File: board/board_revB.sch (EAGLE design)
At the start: 78 parts, among them Q1 ULN2003AS, Q2 ULN2003AD, Y1 8Mhz

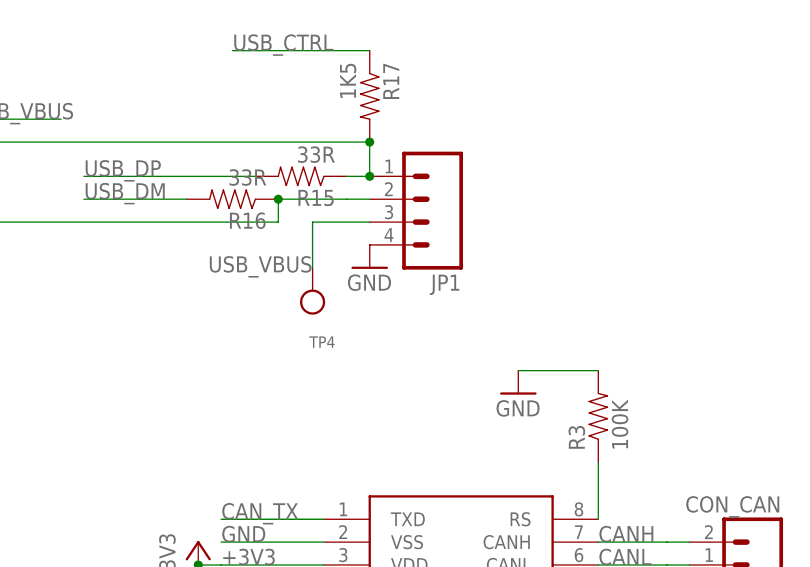
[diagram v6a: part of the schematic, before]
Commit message: [Board Rev B] USB connector renamed.
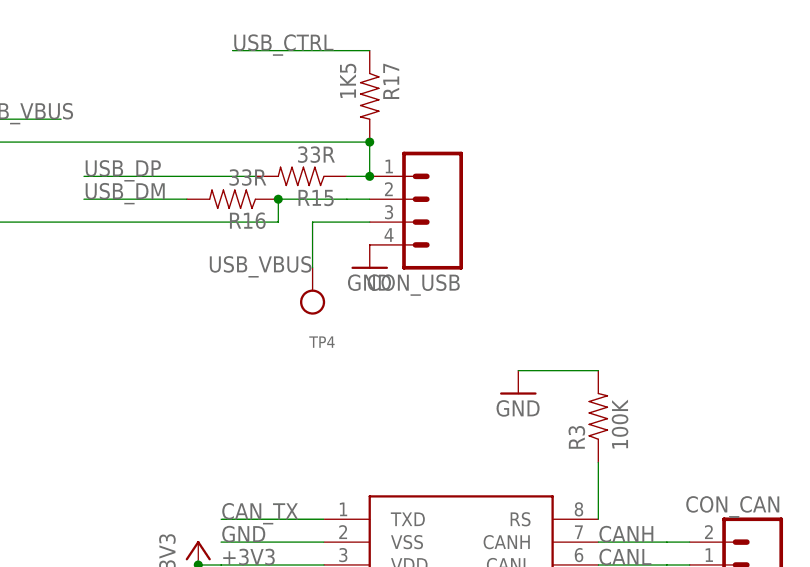
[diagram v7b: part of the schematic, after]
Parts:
- renumbered JP1 to CON_USB
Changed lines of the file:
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@@
 <part name="R22" library="SparkFun-Resistors" deviceset="RESISTOR" device="0603-RES" value="56R"/>
 <part name="R21" library="SparkFun-Resistors" deviceset="RESISTOR" device="0603-RES" value="56R"/>
-<part name="JP1" library="SparkFun-Connectors" deviceset="M04" device="LOCK"/>
+<part name="CON_USB" library="SparkFun-Connectors" deviceset="M04" device="LOCK"/>
 <part name="TP2" library="microbuilder" deviceset="TESTPOINT" device="ROUND1MM"/>
 <part name="TP4" library="microbuilder" deviceset="TESTPOINT" device="ROUND1MM"/>
@@
 <instance part="R22" gate="G$1" x="233.68" y="179.07" rot="R180"/>
 <instance part="R21" gate="G$1" x="242.57" y="176.53" rot="R180"/>
-<instance part="JP1" gate="G$1" x="300.99" y="125.73" rot="R180"/>
+<instance part="CON_USB" gate="G$1" x="300.99" y="125.73" rot="R180"/>
 <instance part="TP2" gate="G$1" x="74.93" y="22.86"/>
 <instance part="TP4" gate="G$1" x="289.56" y="118.11" rot="R180"/>
@@
 <segment>
 <pinref part="GND8" gate="1" pin="GND"/>
-<pinref part="JP1" gate="G$1" pin="4"/>
+<pinref part="CON_USB" gate="G$1" pin="4"/>
 </segment>
 </net>
@@
 <label x="289.56" y="119.38" size="1.778" layer="95" rot="R180"/>
 <wire x1="289.56" y1="123.19" x2="289.56" y2="118.11" width="0.1524" layer="91"/>
-<pinref part="JP1" gate="G$1" pin="3"/>
+<pinref part="CON_USB" gate="G$1" pin="3"/>
 <pinref part="TP4" gate="G$1" pin="P$1"/>
 </segment>
@@
 <wire x1="251.46" y1="129.54" x2="251.46" y2="123.19" width="0.1524" layer="91"/>
 <wire x1="251.46" y1="123.19" x2="285.75" y2="123.19" width="0.1524" layer="91"/>
-<pinref part="JP1" gate="G$1" pin="2"/>
+<pinref part="CON_USB" gate="G$1" pin="2"/>
 </segment>
 </net>
@@
 <wire x1="226.06" y1="132.08" x2="295.91" y2="132.08" width="0.1524" layer="91"/>
 <junction x="295.91" y="132.08"/>
-<pinref part="JP1" gate="G$1" pin="1"/>
+<pinref part="CON_USB" gate="G$1" pin="1"/>
 <junction x="295.91" y="128.27"/>
 </segment>

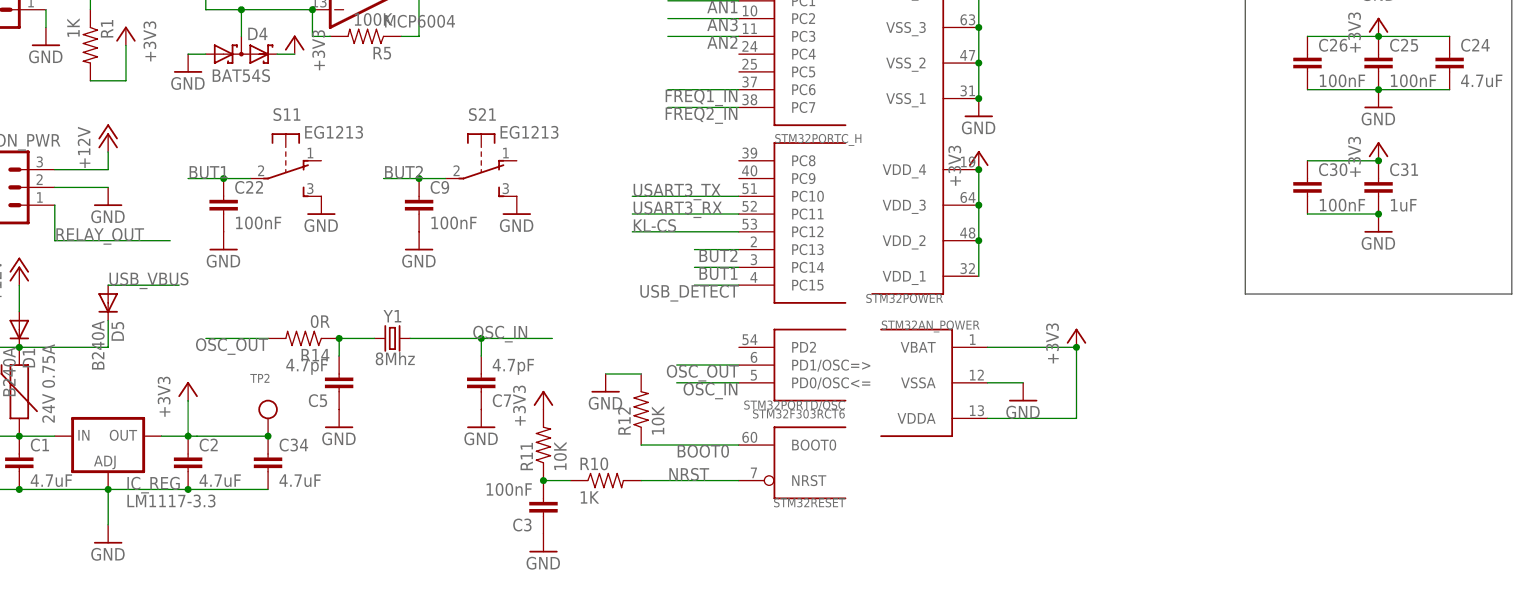
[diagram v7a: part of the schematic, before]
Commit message: [Board Rev B] Adding voltage reference for VDDA.
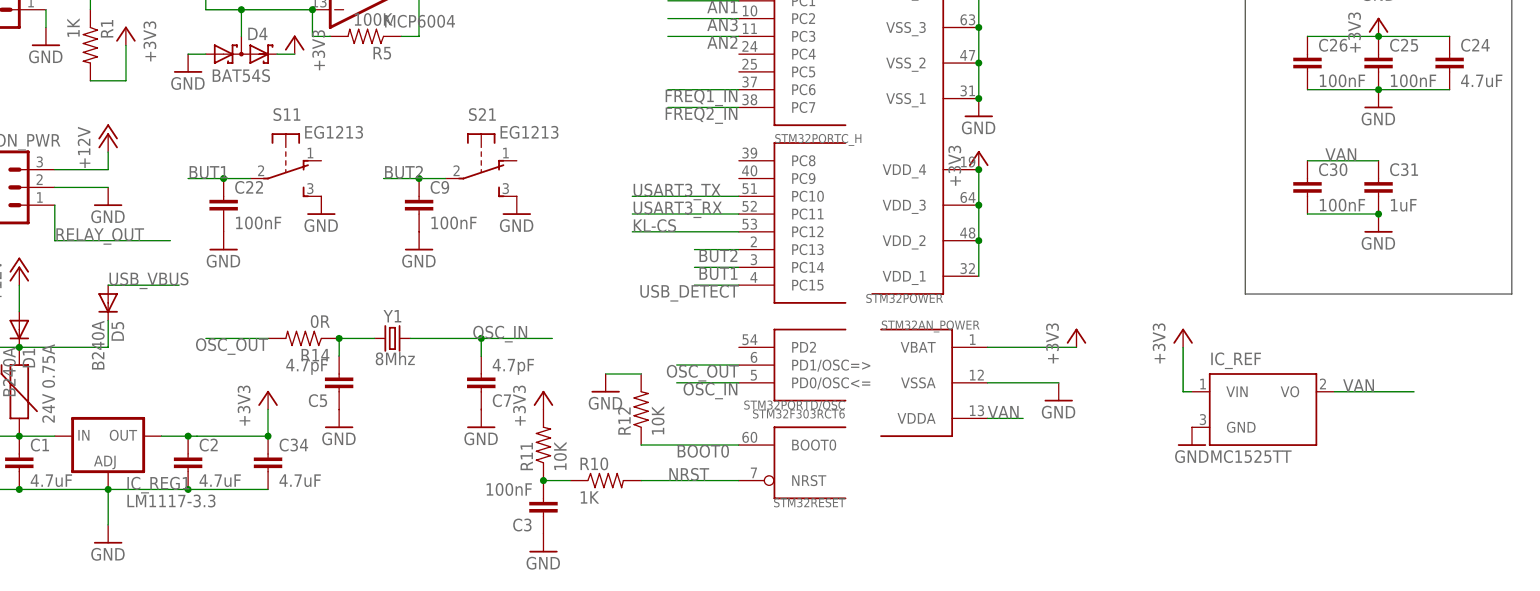
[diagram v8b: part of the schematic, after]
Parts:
- removed TP2: (no value), microbuilder:TESTPOINTROUND1MM
- added IC_REF: MC1525TT, microchip:MC1525TT
- renumbered IC_REG to IC_REG1
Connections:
- new net VAN: C30.1, C31.1, IC_REF.VO, STM32AN_POWER.VDDA
- net +3V3: now also IC_REF.VIN; no longer C30.1, C31.1, STM32AN_POWER.VDDA, TP2.P$1
- net GND: now also IC_REF.GND
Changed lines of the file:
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@@
 </classes>
 <parts>
-<part name="IC_REG" library="v-reg" deviceset="LD117A?*" device="DT" technology="33TR" value="LM1117-3.3"/>
+<part name="IC_REG1" library="v-reg" deviceset="LD117A?*" device="DT" technology="33TR" value="LM1117-3.3"/>
 <part name="GND1" library="supply1" deviceset="GND" device=""/>
-<part name="+3V1" library="supply1" deviceset="+3V3" device=""/>
 <part name="C1" library="SparkFun-Passives" deviceset="CAP" device="0603-CAP" value="4.7uF"/>
 <part name="C2" library="SparkFun-Passives" deviceset="CAP" device="0603-CAP" value="4.7uF"/>
@@
 <part name="C31" library="SparkFun-Capacitors" deviceset="CAP" device="0603-CAP" value="1uF"/>
 <part name="GND33" library="supply1" deviceset="GND" device=""/>
-<part name="+3V15" library="supply1" deviceset="+3V3" device=""/>
 <part name="CON_DBG" library="SparkFun-Connectors" deviceset="M03X2" device="2X3_SILK_SM"/>
 <part name="IC_OPA" library="linear" deviceset="LMV324?*" device="MZ" value="MCP6004"/>
@@
 <part name="R21" library="SparkFun-Resistors" deviceset="RESISTOR" device="0603-RES" value="56R"/>
 <part name="CON_USB" library="SparkFun-Connectors" deviceset="M04" device="LOCK"/>
-<part name="TP2" library="microbuilder" deviceset="TESTPOINT" device="ROUND1MM"/>
 <part name="TP4" library="microbuilder" deviceset="TESTPOINT" device="ROUND1MM"/>
 <part name="F1" library="misc" deviceset="PTC" device="1812K" value="24V 0.75A"/>
+<part name="IC_REF" library="microchip" deviceset="MC15*" device="TT" technology="25"/>
+<part name="GND22" library="supply1" deviceset="GND" device=""/>
+<part name="+3V1" library="supply1" deviceset="+3V3" device=""/>
+<part name="+3V6" library="supply1" deviceset="+3V3" device=""/>
 </parts>
 <sheets>
@@
 </plain>
 <instances>
-<instance part="IC_REG" gate="G$1" x="52.07" y="22.86"/>
+<instance part="IC_REG1" gate="G$1" x="52.07" y="22.86"/>
 <instance part="GND1" gate="1" x="52.07" y="7.62"/>
-<instance part="+3V1" gate="G$1" x="63.5" y="30.48"/>
 <instance part="C1" gate="G$1" x="39.37" y="17.78"/>
 <instance part="C2" gate="G$1" x="63.5" y="17.78"/>
@@
 <instance part="C31" gate="G$1" x="233.68" y="57.15"/>
 <instance part="GND33" gate="1" x="233.68" y="52.07"/>
-<instance part="+3V15" gate="G$1" x="233.68" y="64.77"/>
 <instance part="CON_DBG" gate="G$1" x="133.35" y="152.4"/>
 <instance part="IC_OPA" gate="P" x="110.49" y="114.3"/>
@@
 <instance part="IC_OPA" gate="A" x="87.63" y="148.59"/>
 <instance part="IC_OPA" gate="B" x="73.66" y="106.68"/>
-<instance part="GND3" gate="1" x="182.88" y="27.94"/>
+<instance part="GND3" gate="1" x="187.96" y="27.94"/>
 <instance part="GND7" gate="1" x="44.45" y="113.03"/>
 <instance part="+3V2" gate="G$1" x="190.5" y="38.1"/>
@@
 <instance part="R21" gate="G$1" x="242.57" y="176.53" rot="R180"/>
 <instance part="CON_USB" gate="G$1" x="300.99" y="125.73" rot="R180"/>
-<instance part="TP2" gate="G$1" x="74.93" y="22.86"/>
 <instance part="TP4" gate="G$1" x="289.56" y="118.11" rot="R180"/>
 <instance part="F1" gate="G$1" x="39.37" y="27.94" rot="R90"/>
+<instance part="IC_REF" gate="G$1" x="217.17" y="26.67"/>
+<instance part="GND22" gate="1" x="207.01" y="21.59"/>
+<instance part="+3V1" gate="G$1" x="205.74" y="38.1"/>
+<instance part="+3V6" gate="G$1" x="74.93" y="29.21"/>
 </instances>
 <busses>
@@
 <net name="GND" class="0">
 <segment>
-<pinref part="IC_REG" gate="G$1" pin="ADJ"/>
+<pinref part="IC_REG1" gate="G$1" pin="ADJ"/>
 <wire x1="52.07" y1="15.24" x2="52.07" y2="10.16" width="0.1524" layer="91"/>
 <pinref part="GND1" gate="1" pin="GND"/>
@@
 <pinref part="GND3" gate="1" pin="GND"/>
 <pinref part="STM32" gate="AN_POWER" pin="VSSA"/>
-<wire x1="182.88" y1="30.48" x2="177.8" y2="30.48" width="0.1524" layer="91"/>
+<wire x1="187.96" y1="30.48" x2="177.8" y2="30.48" width="0.1524" layer="91"/>
 </segment>
 <segment>
@@
 <pinref part="CON_USB" gate="G$1" pin="4"/>
 </segment>
+<segment>
+<pinref part="IC_REF" gate="G$1" pin="GND"/>
+<pinref part="GND22" gate="1" pin="GND"/>
+</segment>
 </net>
 <net name="+3V3" class="0">
-<segment>
-<pinref part="IC_REG" gate="G$1" pin="OUT"/>
-<wire x1="59.69" y1="22.86" x2="63.5" y2="22.86" width="0.1524" layer="91"/>
-<pinref part="+3V1" gate="G$1" pin="+3V3"/>
-<wire x1="63.5" y1="27.94" x2="63.5" y2="22.86" width="0.1524" layer="91"/>
-<pinref part="C2" gate="G$1" pin="1"/>
-<junction x="63.5" y="22.86"/>
-<pinref part="C34" gate="G$1" pin="1"/>
-<wire x1="64.77" y1="22.86" x2="74.93" y2="22.86" width="0.1524" layer="91"/>
-<wire x1="64.77" y1="22.86" x2="63.5" y2="22.86" width="0.1524" layer="91"/>
-<pinref part="TP2" gate="G$1" pin="P$1"/>
-<junction x="74.93" y="22.86"/>
-</segment>
 <segment>
 <pinref part="C24" gate="G$1" pin="1"/>
@@
 <junction x="233.68" y="97.79"/>
 <pinref part="C28" gate="G$1" pin="1"/>
-</segment>
-<segment>
-<pinref part="C30" gate="G$1" pin="1"/>
-<pinref part="C31" gate="G$1" pin="1"/>
-<wire x1="223.52" y1="62.23" x2="233.68" y2="62.23" width="0.1524" layer="91"/>
-<pinref part="+3V15" gate="G$1" pin="+3V3"/>
-<junction x="233.68" y="62.23"/>
 </segment>
 <segment>
@@
 </segment>
 <segment>
-<pinref part="STM32" gate="AN_POWER" pin="VDDA"/>
-<wire x1="177.8" y1="25.4" x2="190.5" y2="25.4" width="0.1524" layer="91"/>
+<pinref part="+3V1" gate="G$1" pin="+3V3"/>
+<pinref part="IC_REF" gate="G$1" pin="VIN"/>
+<wire x1="207.01" y1="29.21" x2="205.74" y2="29.21" width="0.1524" layer="91"/>
+<wire x1="205.74" y1="29.21" x2="205.74" y2="35.56" width="0.1524" layer="91"/>
+</segment>
+<segment>
 <pinref part="STM32" gate="AN_POWER" pin="VBAT"/>
 <wire x1="177.8" y1="35.56" x2="190.5" y2="35.56" width="0.1524" layer="91"/>
-<wire x1="190.5" y1="35.56" x2="190.5" y2="25.4" width="0.1524" layer="91"/>
 <pinref part="+3V2" gate="G$1" pin="+3V3"/>
-<junction x="190.5" y="35.56"/>
 </segment>
 <segment>
@@
 <pinref part="R2" gate="G$1" pin="2"/>
 <pinref part="+3V11" gate="G$1" pin="+3V3"/>
+</segment>
+<segment>
+<pinref part="IC_REG1" gate="G$1" pin="OUT"/>
+<wire x1="59.69" y1="22.86" x2="63.5" y2="22.86" width="0.1524" layer="91"/>
+<pinref part="C2" gate="G$1" pin="1"/>
+<junction x="63.5" y="22.86"/>
+<pinref part="C34" gate="G$1" pin="1"/>
+<wire x1="64.77" y1="22.86" x2="74.93" y2="22.86" width="0.1524" layer="91"/>
+<wire x1="64.77" y1="22.86" x2="63.5" y2="22.86" width="0.1524" layer="91"/>
+<wire x1="74.93" y1="22.86" x2="74.93" y2="26.67" width="0.1524" layer="91"/>
+<junction x="74.93" y="22.86"/>
+<pinref part="+3V6" gate="G$1" pin="+3V3"/>
 </segment>
 </net>
@@
 <net name="N$20" class="0">
 <segment>
-<pinref part="IC_REG" gate="G$1" pin="IN"/>
+<pinref part="IC_REG1" gate="G$1" pin="IN"/>
 <wire x1="44.45" y1="22.86" x2="39.37" y2="22.86" width="0.1524" layer="91"/>
 <pinref part="C1" gate="G$1" pin="1"/>
@@
 </segment>
 </net>
+<net name="VAN" class="0">
+<segment>
+<pinref part="STM32" gate="AN_POWER" pin="VDDA"/>
+<wire x1="177.8" y1="25.4" x2="182.88" y2="25.4" width="0.1524" layer="91"/>
+<label x="177.8" y="25.4" size="1.778" layer="95"/>
+</segment>
+<segment>
+<pinref part="IC_REF" gate="G$1" pin="VO"/>
+<wire x1="227.33" y1="29.21" x2="238.76" y2="29.21" width="0.1524" layer="91"/>
+<label x="228.6" y="29.21" size="1.778" layer="95"/>
+</segment>
+<segment>
+<pinref part="C30" gate="G$1" pin="1"/>
+<pinref part="C31" gate="G$1" pin="1"/>
+<wire x1="223.52" y1="62.23" x2="233.68" y2="62.23" width="0.1524" layer="91"/>
+<label x="226.06" y="62.23" size="1.778" layer="95"/>
+</segment>
+</net>
